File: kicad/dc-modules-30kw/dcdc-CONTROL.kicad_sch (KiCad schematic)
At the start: 35 parts

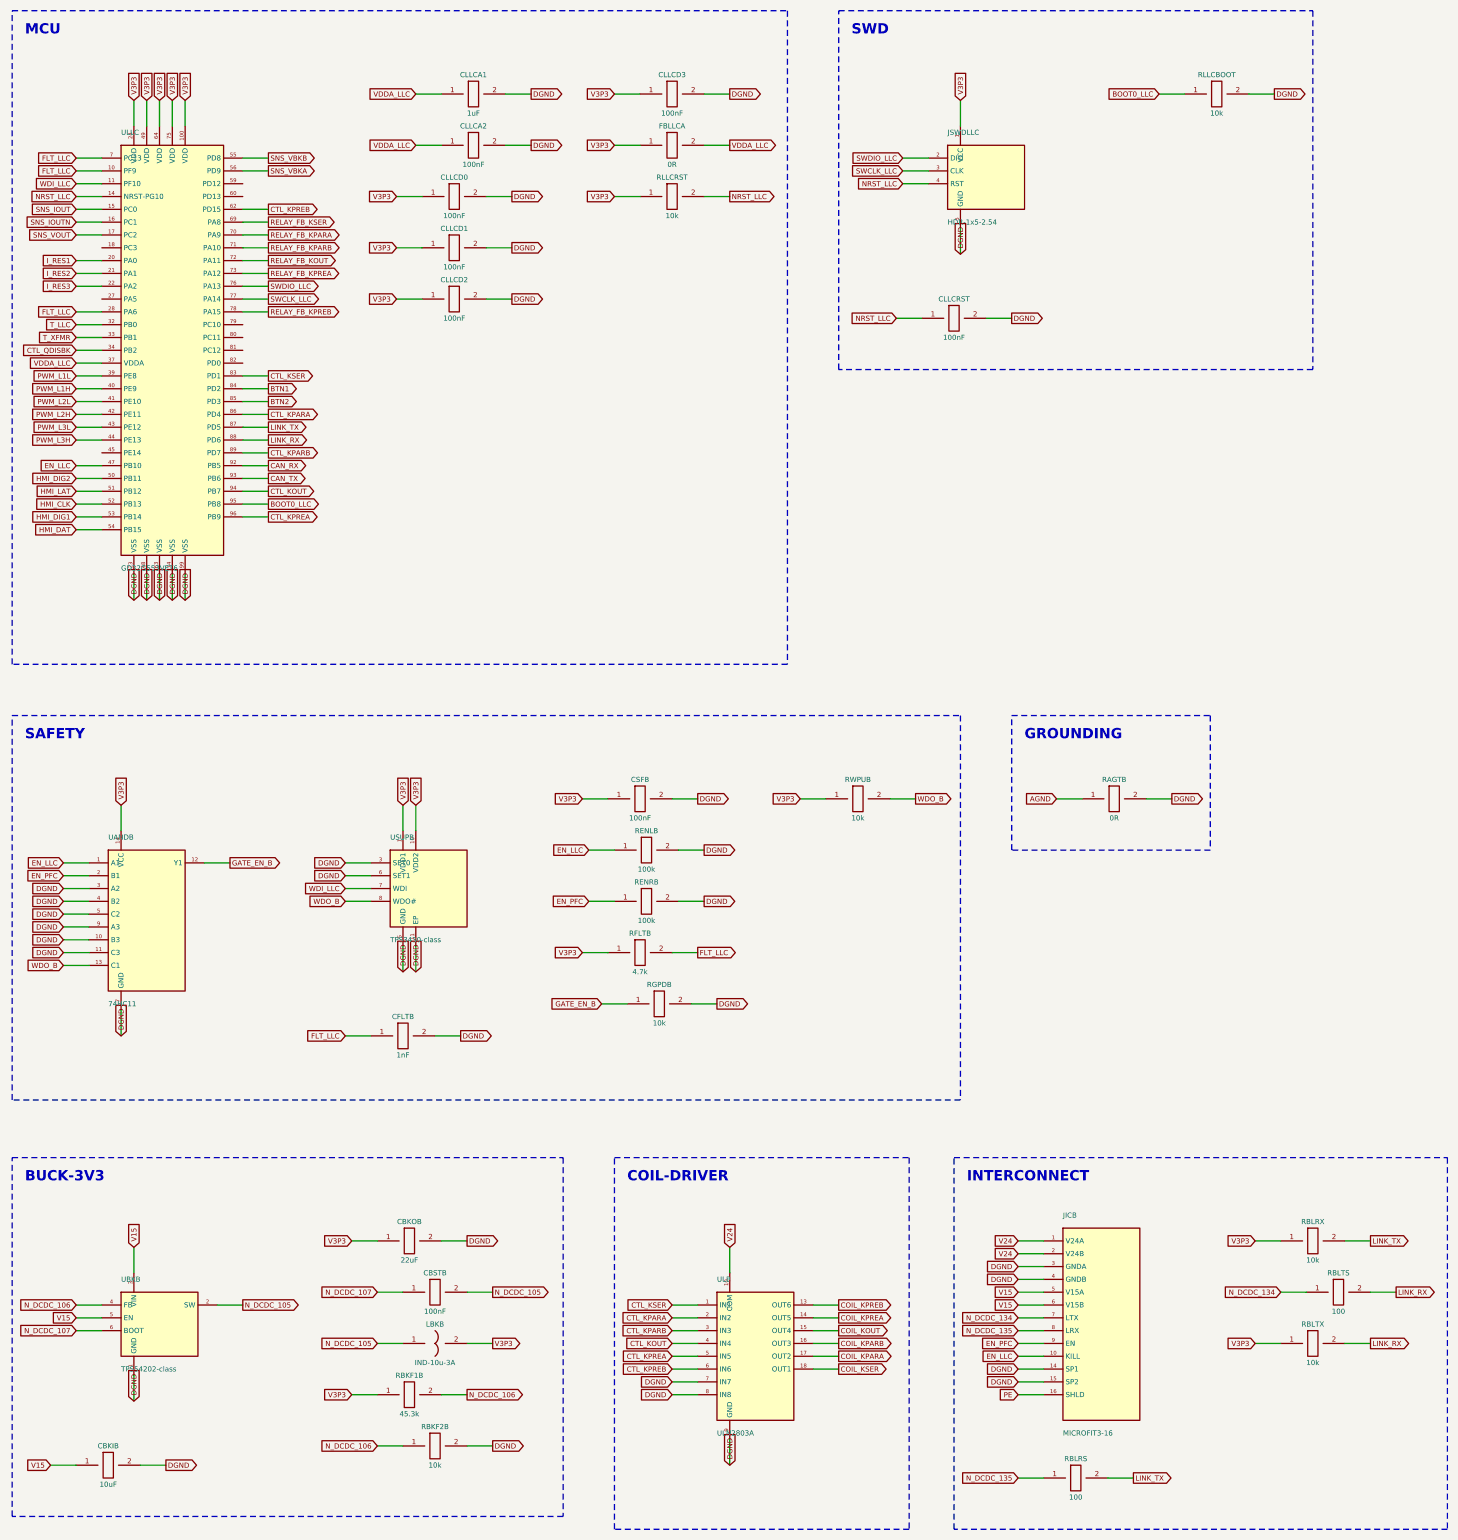
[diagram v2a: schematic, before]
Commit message: Visual pass on the hand-placed sheets: four draughting defects fixed
End-to-end inspection at zoom found four things the wide view hides:

1. The reference designator collided with the first top pin's number on
   every multi-pin IC. The library default had been moved but the INSTANCE
   property is what renders -- fixed there, right-justified clear of the body.
2. Power pins on the top/bottom edges drew their name INSIDE the body,
   rotated, straight through the first left/right pin name (VDD over PC13 on
   the MCU). Their names are now suppressed; the net label outside already
   says V3P3 / DGND, which is standard practice on a large MCU.
3. Unbound symbol pins rendered as bare stubs that read as unfinished
   connections. Every one now carries an explicit no-connect marker.
4. Single-pin parts (M8 studs, heatsink tab) were drawn by the IC path as
   large empty rectangles. They now use a real terminal symbol -- a small
   open circle on a stub -- in both the KiCad 10 and legacy generators.

Both verifiers still 100.00% (1735/1735 pins, 608 components, 0 floating
labels, 0 overlapping symbols, 0 unclosed frames). Page PDFs and the EasyEDA
import bundle regenerated against the corrected MCU pin map.

Co-Authored-By: Claude Fable 5 <noreply@anthropic.com>
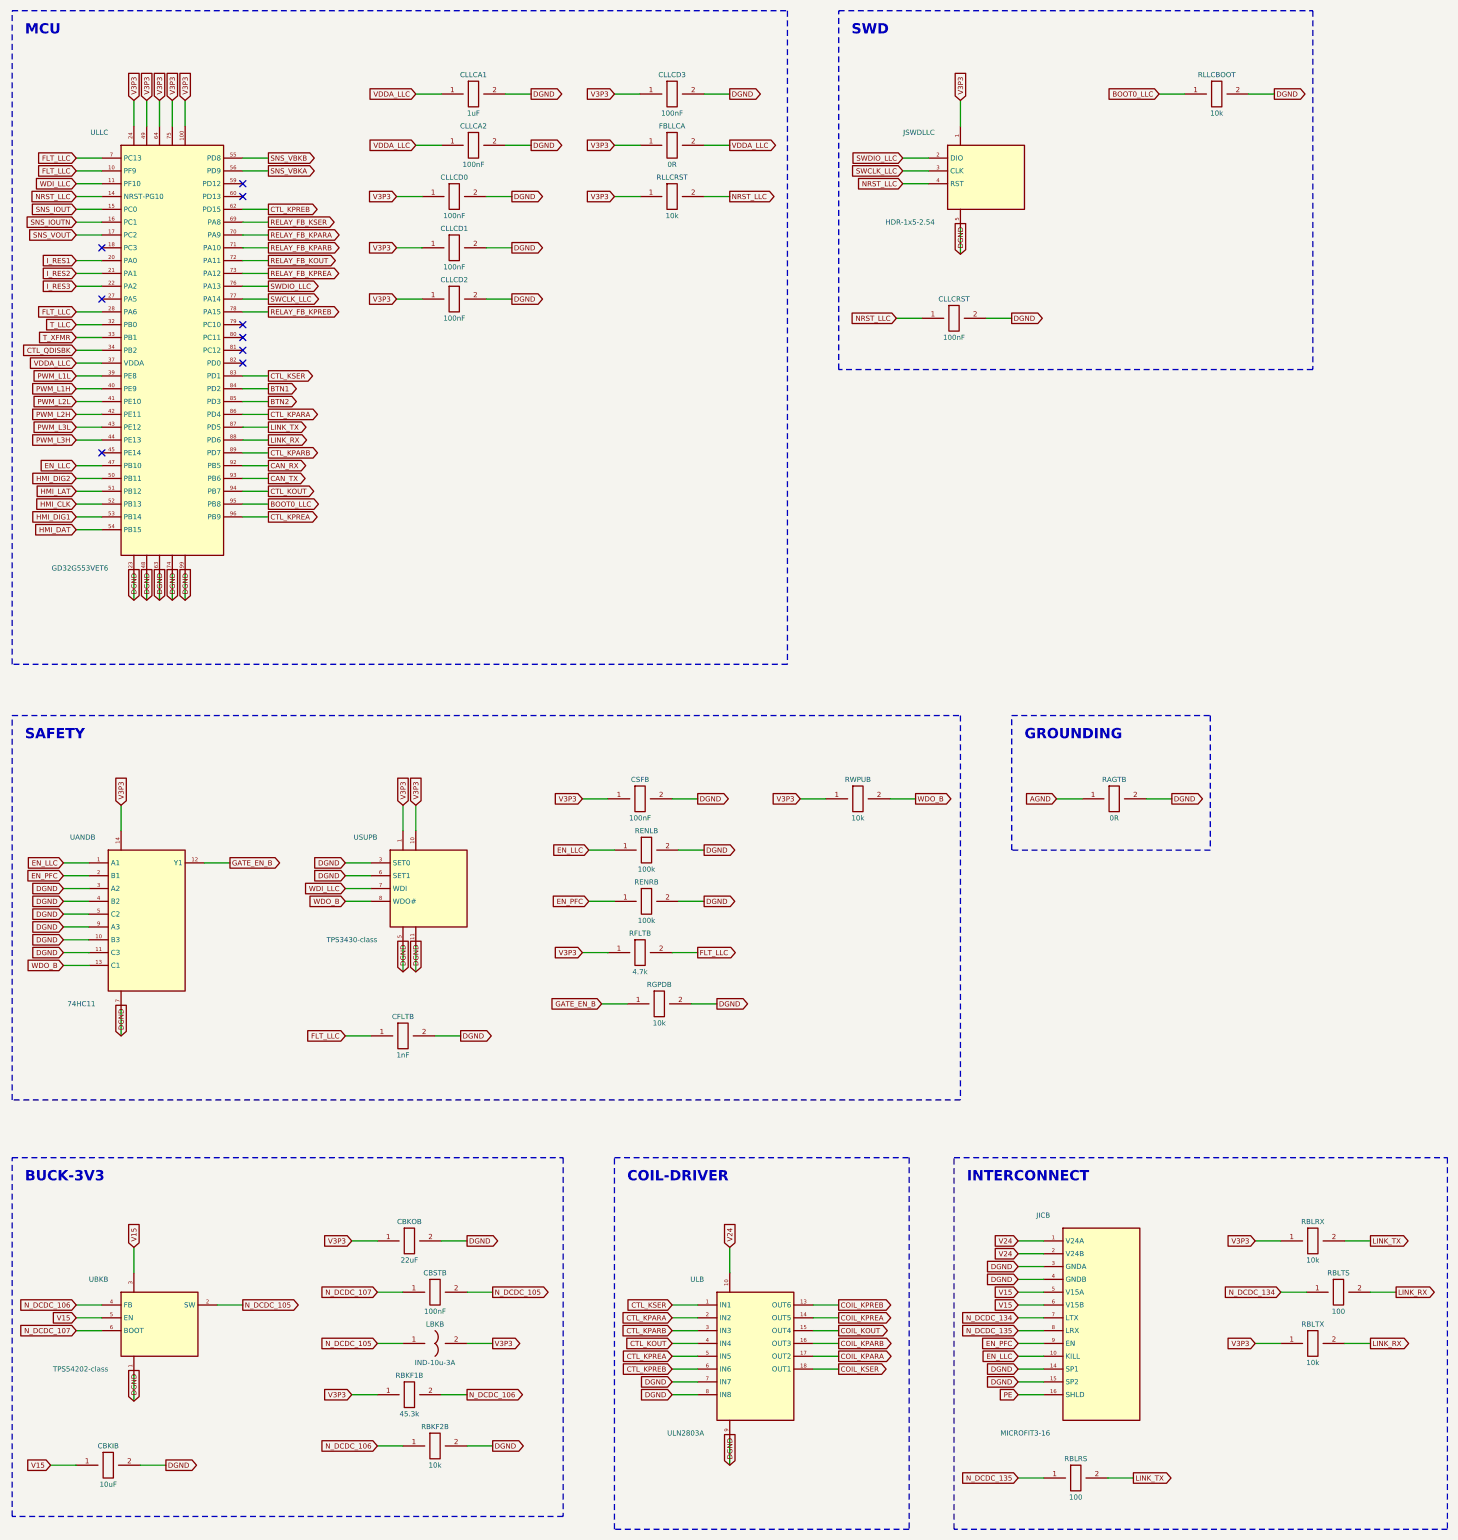
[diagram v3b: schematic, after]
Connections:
- no-connect marks 0 -> 9
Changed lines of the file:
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@@
 	(symbol (lib_id "dc-modules:GD32G553VET6") (at 44.45 80.01 0) (unit 1)
 		(exclude_from_sim no) (in_bom yes) (on_board yes) (dnp no)
-		(property "Reference" "ULLC" (at 34.29 36.83 0) (effects (font (size 1.016 1.016)) (justify left)))
-		(property "Value" "GD32G553VET6" (at 34.29 123.19 0) (effects (font (size 1.016 1.016)) (justify left)))
+		(property "Reference" "ULLC" (at 31.75 36.83 0) (effects (font (size 1.016 1.016)) (justify right)))
+		(property "Value" "GD32G553VET6" (at 31.75 123.19 0) (effects (font (size 1.016 1.016)) (justify right)))
 		(property "LCSC" "" (at 44.45 80.01 0) (effects (font (size 1.016 1.016)) (hide yes)))
 		(instances (project "dc-modules-30kw" (path "/1137c544-07da-408a-a42a-9b4ef459ff51" (reference "ULLC") (unit 1)))))
@@
 	(global_label "SNS_VOUT" (shape input) (at 25.4 57.15 180)
 		(effects (font (size 1.016 1.016)) (justify right)))
+	(no_connect (at 30.48 59.69))
 	(wire (pts (xy 30.48 62.230000000000004) (xy 25.4 62.230000000000004)) (stroke (width 0) (type default)))
 	(global_label "I_RES1" (shape input) (at 25.4 62.230000000000004 180)
@@
 	(global_label "I_RES3" (shape input) (at 25.4 67.31 180)
 		(effects (font (size 1.016 1.016)) (justify right)))
+	(no_connect (at 30.48 69.85))
 	(wire (pts (xy 30.48 72.39) (xy 25.4 72.39)) (stroke (width 0) (type default)))
 	(global_label "FLT_LLC" (shape input) (at 25.4 72.39 180)
@@
 	(global_label "PWM_L3H" (shape input) (at 25.4 97.79 180)
 		(effects (font (size 1.016 1.016)) (justify right)))
+	(no_connect (at 30.48 100.33))
 	(wire (pts (xy 30.48 102.87) (xy 25.4 102.87)) (stroke (width 0) (type default)))
 	(global_label "EN_LLC" (shape input) (at 25.4 102.87 180)
@@
 	(global_label "SNS_VBKA" (shape output) (at 63.5 44.45 0)
 		(effects (font (size 1.016 1.016)) (justify left)))
+	(no_connect (at 58.42 46.99))
+	(no_connect (at 58.42 49.53))
 	(wire (pts (xy 58.42 52.07) (xy 63.5 52.07)) (stroke (width 0) (type default)))
 	(global_label "CTL_KPREB" (shape output) (at 63.5 52.07 0)
@@
 	(global_label "RELAY_FB_KPREB" (shape output) (at 63.5 72.39 0)
 		(effects (font (size 1.016 1.016)) (justify left)))
+	(no_connect (at 58.42 74.93))
+	(no_connect (at 58.42 77.47))
+	(no_connect (at 58.42 80.01))
+	(no_connect (at 58.42 82.55))
 	(wire (pts (xy 58.42 85.09) (xy 63.5 85.09)) (stroke (width 0) (type default)))
 	(global_label "CTL_KSER" (shape output) (at 63.5 85.09 0)
@@
 	(symbol (lib_id "dc-modules:HDR-1x5-2.54") (at 205.74 45.72 0) (unit 1)
 		(exclude_from_sim no) (in_bom yes) (on_board yes) (dnp no)
-		(property "Reference" "JSWDLLC" (at 198.12 36.83 0) (effects (font (size 1.016 1.016)) (justify left)))
-		(property "Value" "HDR-1x5-2.54" (at 198.12 54.61 0) (effects (font (size 1.016 1.016)) (justify left)))
+		(property "Reference" "JSWDLLC" (at 195.58 36.83 0) (effects (font (size 1.016 1.016)) (justify right)))
+		(property "Value" "HDR-1x5-2.54" (at 195.58 54.61 0) (effects (font (size 1.016 1.016)) (justify right)))
 		(property "LCSC" "" (at 205.74 45.72 0) (effects (font (size 1.016 1.016)) (hide yes)))
 		(instances (project "dc-modules-30kw" (path "/1137c544-07da-408a-a42a-9b4ef459ff51" (reference "JSWDLLC") (unit 1)))))
@@
 	(symbol (lib_id "dc-modules:74HC11") (at 39.37 193.04 0) (unit 1)
 		(exclude_from_sim no) (in_bom yes) (on_board yes) (dnp no)
-		(property "Reference" "UANDB" (at 31.75 176.53 0) (effects (font (size 1.016 1.016)) (justify left)))
-		(property "Value" "74HC11" (at 31.75 209.55 0) (effects (font (size 1.016 1.016)) (justify left)))
+		(property "Reference" "UANDB" (at 29.21 176.53 0) (effects (font (size 1.016 1.016)) (justify right)))
+		(property "Value" "74HC11" (at 29.21 209.55 0) (effects (font (size 1.016 1.016)) (justify right)))
 		(property "LCSC" "" (at 39.37 193.04 0) (effects (font (size 1.016 1.016)) (hide yes)))
 		(instances (project "dc-modules-30kw" (path "/1137c544-07da-408a-a42a-9b4ef459ff51" (reference "UANDB") (unit 1)))))
@@
 	(symbol (lib_id "dc-modules:TPS3430-class") (at 95.25 186.69 0) (unit 1)
 		(exclude_from_sim no) (in_bom yes) (on_board yes) (dnp no)
-		(property "Reference" "USUPB" (at 87.63 176.53 0) (effects (font (size 1.016 1.016)) (justify left)))
-		(property "Value" "TPS3430-class" (at 87.63 196.85 0) (effects (font (size 1.016 1.016)) (justify left)))
+		(property "Reference" "USUPB" (at 85.09 176.53 0) (effects (font (size 1.016 1.016)) (justify right)))
+		(property "Value" "TPS3430-class" (at 85.09 196.85 0) (effects (font (size 1.016 1.016)) (justify right)))
 		(property "LCSC" "" (at 95.25 186.69 0) (effects (font (size 1.016 1.016)) (hide yes)))
 		(instances (project "dc-modules-30kw" (path "/1137c544-07da-408a-a42a-9b4ef459ff51" (reference "USUPB") (unit 1)))))
@@
 	(symbol (lib_id "dc-modules:TPS54202-class") (at 41.910000000000004 273.05 0) (unit 1)
 		(exclude_from_sim no) (in_bom yes) (on_board yes) (dnp no)
-		(property "Reference" "UBKB" (at 34.29 264.16 0) (effects (font (size 1.016 1.016)) (justify left)))
-		(property "Value" "TPS54202-class" (at 34.29 281.94 0) (effects (font (size 1.016 1.016)) (justify left)))
+		(property "Reference" "UBKB" (at 31.75 264.16 0) (effects (font (size 1.016 1.016)) (justify right)))
+		(property "Value" "TPS54202-class" (at 31.75 281.94 0) (effects (font (size 1.016 1.016)) (justify right)))
 		(property "LCSC" "" (at 41.910000000000004 273.05 0) (effects (font (size 1.016 1.016)) (hide yes)))
 		(instances (project "dc-modules-30kw" (path "/1137c544-07da-408a-a42a-9b4ef459ff51" (reference "UBKB") (unit 1)))))
@@
 	(symbol (lib_id "dc-modules:ULN2803A") (at 160.02 279.4 0) (unit 1)
 		(exclude_from_sim no) (in_bom yes) (on_board yes) (dnp no)
-		(property "Reference" "ULB" (at 152.4 264.16 0) (effects (font (size 1.016 1.016)) (justify left)))
-		(property "Value" "ULN2803A" (at 152.4 294.64 0) (effects (font (size 1.016 1.016)) (justify left)))
+		(property "Reference" "ULB" (at 149.86 264.16 0) (effects (font (size 1.016 1.016)) (justify right)))
+		(property "Value" "ULN2803A" (at 149.86 294.64 0) (effects (font (size 1.016 1.016)) (justify right)))
 		(property "LCSC" "" (at 160.02 279.4 0) (effects (font (size 1.016 1.016)) (hide yes)))
 		(instances (project "dc-modules-30kw" (path "/1137c544-07da-408a-a42a-9b4ef459ff51" (reference "ULB") (unit 1)))))
@@
 	(symbol (lib_id "dc-modules:MICROFIT3-16") (at 228.6 273.05 0) (unit 1)
 		(exclude_from_sim no) (in_bom yes) (on_board yes) (dnp no)
-		(property "Reference" "JICB" (at 220.98 251.46 0) (effects (font (size 1.016 1.016)) (justify left)))
-		(property "Value" "MICROFIT3-16" (at 220.98 294.64 0) (effects (font (size 1.016 1.016)) (justify left)))
+		(property "Reference" "JICB" (at 218.44 251.46 0) (effects (font (size 1.016 1.016)) (justify right)))
+		(property "Value" "MICROFIT3-16" (at 218.44 294.64 0) (effects (font (size 1.016 1.016)) (justify right)))
 		(property "LCSC" "" (at 228.6 273.05 0) (effects (font (size 1.016 1.016)) (hide yes)))
 		(instances (project "dc-modules-30kw" (path "/1137c544-07da-408a-a42a-9b4ef459ff51" (reference "JICB") (unit 1)))))
